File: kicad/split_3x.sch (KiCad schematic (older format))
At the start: 64 parts, among them SW1 SW_Push, SW2 SW_Push, SW3 Rotary_Encoder_Switch, SW4 Rotary_Encoder_Switch, U1 ProMicro, U2 TRRS

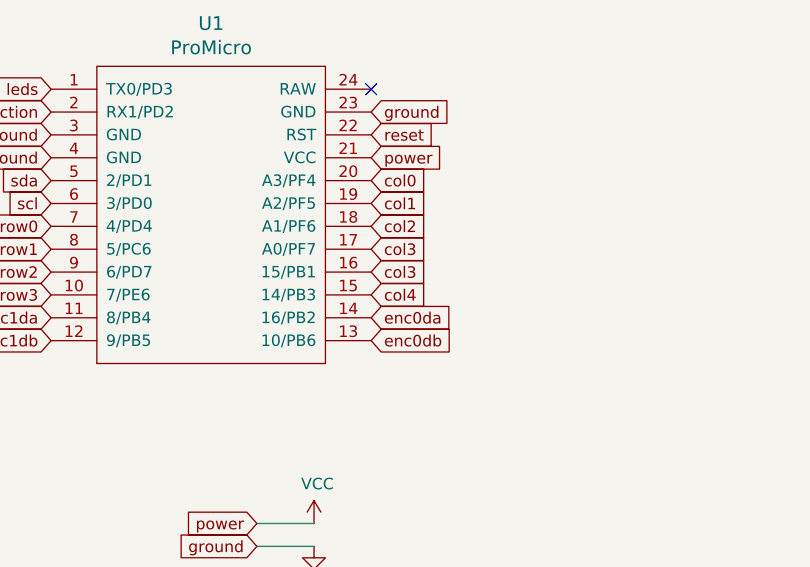
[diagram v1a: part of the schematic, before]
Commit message: added some routing
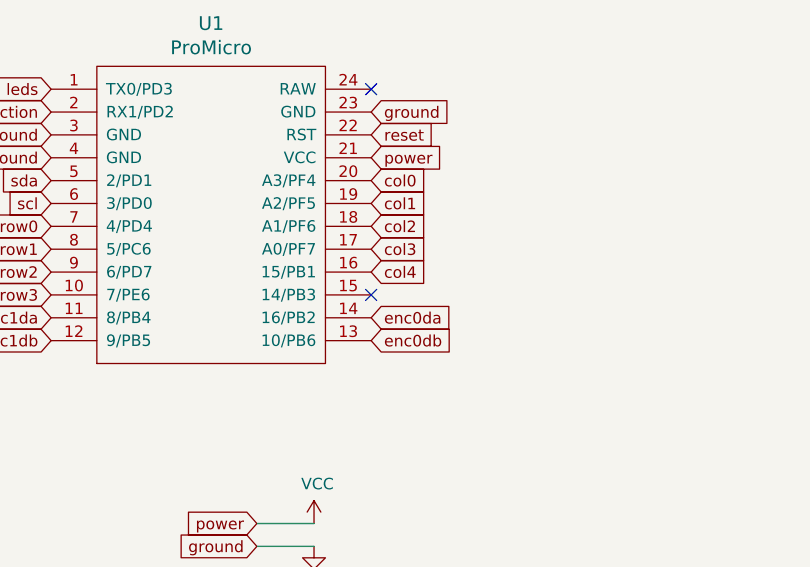
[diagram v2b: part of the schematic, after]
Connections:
- net col3: no longer U1.16 (15/PB1)
- net col4: now also U1.16 (15/PB1); no longer U1.15 (14/PB3)
- no-connect marks 3 -> 4
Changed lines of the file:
@@
 col3
 Text GLabel 2750 2250 2    50   Input ~ 0
-col3
-Text GLabel 2750 2350 2    50   Input ~ 0
 col4
 Text GLabel 1350 2050 0    50   Input ~ 0
@@
 Text GLabel 9750 2250 0    50   Input ~ 0
 power
+NoConn ~ 2750 2350
 $EndSCHEMATC

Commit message: finished routing
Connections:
- net leds: now also D29.4 (DIN); no longer D20.4 (DIN)
- net at D28.2 (DOUT): no longer D29.4 (DIN)
- net at D29.2 (DOUT): now also D20.4 (DIN)
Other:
- moved on the sheet: D29
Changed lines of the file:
@@
 L LED:WS2812B D29
 U 1 1 5FD20037
-P 9650 5550
-F 0 "D29" H 9994 5596 50  0000 L CNN
-F 1 "WS2812B" H 9994 5505 50  0000 L CNN
-F 2 "Keebio-Parts:WS2812B" H 9700 5250 50  0001 L TNN
-F 3 "https://cdn-shop.adafruit.com/datasheets/WS2812B.pdf" H 9750 5175 50  0001 L TNN
-	1    9650 5550
+P 3650 5550
+F 0 "D29" H 3994 5596 50  0000 L CNN
+F 1 "WS2812B" H 3994 5505 50  0000 L CNN
+F 2 "Keebio-Parts:WS2812B" H 3700 5250 50  0001 L TNN
+F 3 "https://cdn-shop.adafruit.com/datasheets/WS2812B.pdf" H 3750 5175 50  0001 L TNN
+	1    3650 5550
 	1    0    0    -1
 $EndComp
@@
 L power:GND #PWR024
 U 1 1 5FD489BC
-P 9650 5850
-F 0 "#PWR024" H 9650 5600 50  0001 C CNN
-F 1 "GND" H 9655 5677 50  0000 C CNN
-F 2 "" H 9650 5850 50  0001 C CNN
-F 3 "" H 9650 5850 50  0001 C CNN
-	1    9650 5850
+P 3650 5850
+F 0 "#PWR024" H 3650 5600 50  0001 C CNN
+F 1 "GND" H 3655 5677 50  0000 C CNN
+F 2 "" H 3650 5850 50  0001 C CNN
+F 3 "" H 3650 5850 50  0001 C CNN
+	1    3650 5850
 	1    0    0    -1
 $EndComp
@@
 L power:VCC #PWR023
 U 1 1 5FD53615
-P 9650 5250
-F 0 "#PWR023" H 9650 5100 50  0001 C CNN
-F 1 "VCC" H 9665 5423 50  0000 C CNN
-F 2 "" H 9650 5250 50  0001 C CNN
-F 3 "" H 9650 5250 50  0001 C CNN
-	1    9650 5250
+P 3650 5250
+F 0 "#PWR023" H 3650 5100 50  0001 C CNN
+F 1 "VCC" H 3665 5423 50  0000 C CNN
+F 2 "" H 3650 5250 50  0001 C CNN
+F 3 "" H 3650 5250 50  0001 C CNN
+	1    3650 5250
 	1    0    0    -1
 $EndComp
 NoConn ~ 9950 5550
-Text GLabel 3950 5550 0    50   Input ~ 0
+Text GLabel 3350 5550 0    50   Input ~ 0
 leds
 $Comp

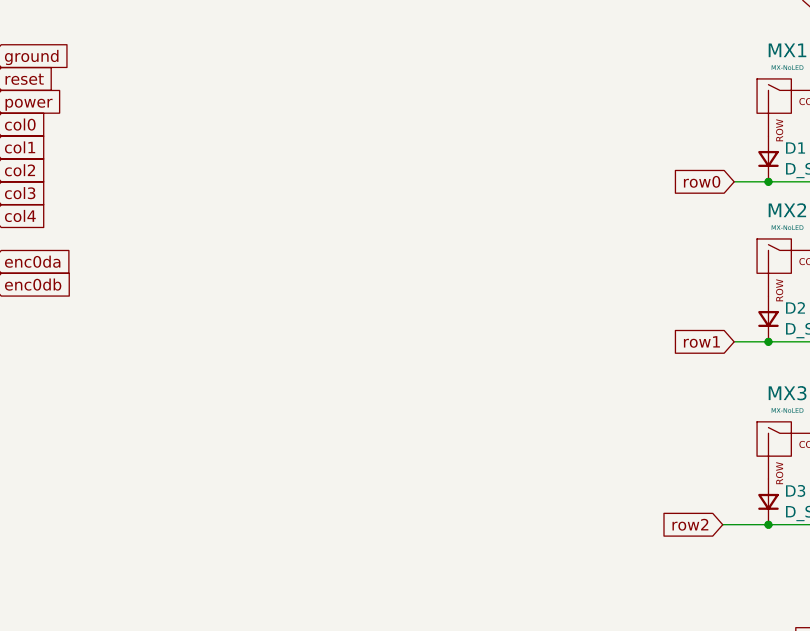
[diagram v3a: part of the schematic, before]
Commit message: added support for the pimoroni trackball breakout, changed a bunch of things, rewired the pcb, changed the bottom plate to be prettier, added some silkscreen, changed the position of one of the mounting holes, changed the angle of the trrs jacks to be properly aligned, changed the top plate to look better
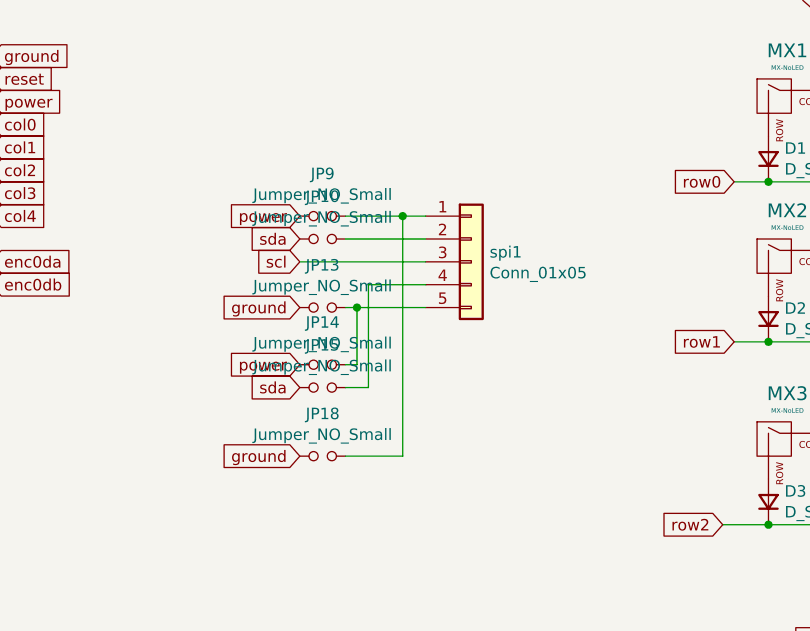
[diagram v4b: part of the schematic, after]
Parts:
- added JP10, JP13, JP14, JP15, JP18, JP9: Jumper_NO_Small, Jumper:SolderJumper-2_P1.3mm_Open_RoundedPad1.0x1.5mm, symbol Device:Jumper_NO_Small
- added spi1: Conn_01x05, other_parts:pimoroni_left_side_mount, symbol Connector_Generic:Conn_01x05
- D1, D10, D11, D12, D13, D14, D15, D16, D17, D18, D19, D2, D3, D4, D5, D6, D7, D8, D9: footprint Keebio-Parts:D_SOD-323 -> Keebio-Parts:D_SOD123F
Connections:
- net GND: now also JP13.1, JP18.1
- net VCC: now also JP14.1, JP9.1
- net scl: now also spi1.3 (Pin_3)
- net sda: now also JP10.1, JP15.1
- new net: JP18.2, JP9.2, spi1.1 (Pin_1)
- new net: JP10.2, spi1.2 (Pin_2)
- new net: JP15.2, spi1.4 (Pin_4)
- new net: JP13.2, JP14.2, spi1.5 (Pin_5)
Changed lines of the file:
@@
 F 0 "D16" V 7846 1930 50  0000 R CNN
 F 1 "D_Small" V 7755 1930 50  0000 R CNN
-F 2 "Keebio-Parts:D_SOD-323" V 7800 2000 50  0001 C CNN
+F 2 "Keebio-Parts:D_SOD123F" V 7800 2000 50  0001 C CNN
 F 3 "~" V 7800 2000 50  0001 C CNN
 	1    7800 2000
@@
 F 0 "D12" V 7446 1930 50  0000 R CNN
 F 1 "D_Small" V 7355 1930 50  0000 R CNN
-F 2 "Keebio-Parts:D_SOD-323" V 7400 2000 50  0001 C CNN
+F 2 "Keebio-Parts:D_SOD123F" V 7400 2000 50  0001 C CNN
 F 3 "~" V 7400 2000 50  0001 C CNN
 	1    7400 2000
@@
 F 0 "D8" V 7046 1930 50  0000 R CNN
 F 1 "D_Small" V 6955 1930 50  0000 R CNN
-F 2 "Keebio-Parts:D_SOD-323" V 7000 2000 50  0001 C CNN
+F 2 "Keebio-Parts:D_SOD123F" V 7000 2000 50  0001 C CNN
 F 3 "~" V 7000 2000 50  0001 C CNN
 	1    7000 2000
@@
 F 0 "D4" V 6646 1930 50  0000 R CNN
 F 1 "D_Small" V 6555 1930 50  0000 R CNN
-F 2 "Keebio-Parts:D_SOD-323" V 6600 2000 50  0001 C CNN
+F 2 "Keebio-Parts:D_SOD123F" V 6600 2000 50  0001 C CNN
 F 3 "~" V 6600 2000 50  0001 C CNN
 	1    6600 2000
@@
 F 0 "D1" V 6196 1930 50  0000 R CNN
 F 1 "D_Small" V 6105 1930 50  0000 R CNN
-F 2 "Keebio-Parts:D_SOD-323" V 6150 2000 50  0001 C CNN
+F 2 "Keebio-Parts:D_SOD123F" V 6150 2000 50  0001 C CNN
 F 3 "~" V 6150 2000 50  0001 C CNN
 	1    6150 2000
@@
 F 0 "D17" V 7846 2630 50  0000 R CNN
 F 1 "D_Small" V 7755 2630 50  0000 R CNN
-F 2 "Keebio-Parts:D_SOD-323" V 7800 2700 50  0001 C CNN
+F 2 "Keebio-Parts:D_SOD123F" V 7800 2700 50  0001 C CNN
 F 3 "~" V 7800 2700 50  0001 C CNN
 	1    7800 2700
@@
 F 0 "D13" V 7446 2630 50  0000 R CNN
 F 1 "D_Small" V 7355 2630 50  0000 R CNN
-F 2 "Keebio-Parts:D_SOD-323" V 7400 2700 50  0001 C CNN
+F 2 "Keebio-Parts:D_SOD123F" V 7400 2700 50  0001 C CNN
 F 3 "~" V 7400 2700 50  0001 C CNN
 	1    7400 2700
@@
 F 0 "D9" V 7046 2630 50  0000 R CNN
 F 1 "D_Small" V 6955 2630 50  0000 R CNN
-F 2 "Keebio-Parts:D_SOD-323" V 7000 2700 50  0001 C CNN
+F 2 "Keebio-Parts:D_SOD123F" V 7000 2700 50  0001 C CNN
 F 3 "~" V 7000 2700 50  0001 C CNN
 	1    7000 2700
@@
 F 0 "D5" V 6646 2630 50  0000 R CNN
 F 1 "D_Small" V 6555 2630 50  0000 R CNN
-F 2 "Keebio-Parts:D_SOD-323" V 6600 2700 50  0001 C CNN
+F 2 "Keebio-Parts:D_SOD123F" V 6600 2700 50  0001 C CNN
 F 3 "~" V 6600 2700 50  0001 C CNN
 	1    6600 2700
@@
 F 0 "D2" V 6196 2630 50  0000 R CNN
 F 1 "D_Small" V 6105 2630 50  0000 R CNN
-F 2 "Keebio-Parts:D_SOD-323" V 6150 2700 50  0001 C CNN
+F 2 "Keebio-Parts:D_SOD123F" V 6150 2700 50  0001 C CNN
 F 3 "~" V 6150 2700 50  0001 C CNN
 	1    6150 2700
@@
 F 0 "D18" V 7846 3430 50  0000 R CNN
 F 1 "D_Small" V 7755 3430 50  0000 R CNN
-F 2 "Keebio-Parts:D_SOD-323" V 7800 3500 50  0001 C CNN
+F 2 "Keebio-Parts:D_SOD123F" V 7800 3500 50  0001 C CNN
 F 3 "~" V 7800 3500 50  0001 C CNN
 	1    7800 3500
@@
 F 0 "D14" V 7446 3430 50  0000 R CNN
 F 1 "D_Small" V 7355 3430 50  0000 R CNN
-F 2 "Keebio-Parts:D_SOD-323" V 7400 3500 50  0001 C CNN
+F 2 "Keebio-Parts:D_SOD123F" V 7400 3500 50  0001 C CNN
 F 3 "~" V 7400 3500 50  0001 C CNN
 	1    7400 3500
@@
 F 0 "D10" V 7046 3430 50  0000 R CNN
 F 1 "D_Small" V 6955 3430 50  0000 R CNN
-F 2 "Keebio-Parts:D_SOD-323" V 7000 3500 50  0001 C CNN
+F 2 "Keebio-Parts:D_SOD123F" V 7000 3500 50  0001 C CNN
 F 3 "~" V 7000 3500 50  0001 C CNN
 	1    7000 3500
@@
 F 0 "D6" V 6646 3430 50  0000 R CNN
 F 1 "D_Small" V 6555 3430 50  0000 R CNN
-F 2 "Keebio-Parts:D_SOD-323" V 6600 3500 50  0001 C CNN
+F 2 "Keebio-Parts:D_SOD123F" V 6600 3500 50  0001 C CNN
 F 3 "~" V 6600 3500 50  0001 C CNN
 	1    6600 3500
@@
 F 0 "D3" V 6196 3430 50  0000 R CNN
 F 1 "D_Small" V 6105 3430 50  0000 R CNN
-F 2 "Keebio-Parts:D_SOD-323" V 6150 3500 50  0001 C CNN
+F 2 "Keebio-Parts:D_SOD123F" V 6150 3500 50  0001 C CNN
 F 3 "~" V 6150 3500 50  0001 C CNN
 	1    6150 3500
@@
 F 0 "D19" V 7846 4130 50  0000 R CNN
 F 1 "D_Small" V 7755 4130 50  0000 R CNN
-F 2 "Keebio-Parts:D_SOD-323" V 7800 4200 50  0001 C CNN
+F 2 "Keebio-Parts:D_SOD123F" V 7800 4200 50  0001 C CNN
 F 3 "~" V 7800 4200 50  0001 C CNN
 	1    7800 4200
@@
 F 0 "D15" V 7446 4130 50  0000 R CNN
 F 1 "D_Small" V 7355 4130 50  0000 R CNN
-F 2 "Keebio-Parts:D_SOD-323" V 7400 4200 50  0001 C CNN
+F 2 "Keebio-Parts:D_SOD123F" V 7400 4200 50  0001 C CNN
 F 3 "~" V 7400 4200 50  0001 C CNN
 	1    7400 4200
@@
 F 0 "D11" V 7046 4130 50  0000 R CNN
 F 1 "D_Small" V 6955 4130 50  0000 R CNN
-F 2 "Keebio-Parts:D_SOD-323" V 7000 4200 50  0001 C CNN
+F 2 "Keebio-Parts:D_SOD123F" V 7000 4200 50  0001 C CNN
 F 3 "~" V 7000 4200 50  0001 C CNN
 	1    7000 4200
@@
 F 0 "D7" V 6696 4130 50  0000 R CNN
 F 1 "D_Small" V 6605 4130 50  0000 R CNN
-F 2 "Keebio-Parts:D_SOD-323" V 6650 4200 50  0001 C CNN
+F 2 "Keebio-Parts:D_SOD123F" V 6650 4200 50  0001 C CNN
 F 3 "~" V 6650 4200 50  0001 C CNN
 	1    6650 4200
@@
 power
 NoConn ~ 2750 2350
+$Comp
+L Connector_Generic:Conn_01x05 spi1
+U 1 1 5FF77D67
+P 4850 2450
+F 0 "spi1" H 4930 2492 50  0000 L CNN
+F 1 "Conn_01x05" H 4930 2401 50  0000 L CNN
+F 2 "other_parts:pimoroni_left_side_mount" H 4850 2450 50  0001 C CNN
+F 3 "~" H 4850 2450 50  0001 C CNN
+	1    4850 2450
+	1    0    0    -1
+$EndComp
+Text GLabel 4100 2650 0    50   Input ~ 0
+ground
+Text GLabel 4100 2250 0    50   Input ~ 0
+power
+$Comp
+L Device:Jumper_NO_Small JP9
+U 1 1 5FF9B084
+P 4200 2250
+F 0 "JP9" H 4200 2435 50  0000 C CNN
+F 1 "Jumper_NO_Small" H 4200 2344 50  0000 C CNN
+F 2 "Jumper:SolderJumper-2_P1.3mm_Open_RoundedPad1.0x1.5mm" H 4200 2250 50  0001 C CNN
+F 3 "~" H 4200 2250 50  0001 C CNN
+	1    4200 2250
+	1    0    0    -1
+$EndComp
+$Comp
+L Device:Jumper_NO_Small JP10
+U 1 1 5FFA2198
+P 4200 2350
+F 0 "JP10" H 4200 2535 50  0000 C CNN
+F 1 "Jumper_NO_Small" H 4200 2444 50  0000 C CNN
+F 2 "Jumper:SolderJumper-2_P1.3mm_Open_RoundedPad1.0x1.5mm" H 4200 2350 50  0001 C CNN
+F 3 "~" H 4200 2350 50  0001 C CNN
+	1    4200 2350
+	1    0    0    -1
+$EndComp
+$Comp
+L Device:Jumper_NO_Small JP13
+U 1 1 5FFA309F
+P 4200 2650
+F 0 "JP13" H 4200 2835 50  0000 C CNN
+F 1 "Jumper_NO_Small" H 4200 2744 50  0000 C CNN
+F 2 "Jumper:SolderJumper-2_P1.3mm_Open_RoundedPad1.0x1.5mm" H 4200 2650 50  0001 C CNN
+F 3 "~" H 4200 2650 50  0001 C CNN
+	1    4200 2650
+	1    0    0    -1
+$EndComp
+$Comp
+L Device:Jumper_NO_Small JP14
+U 1 1 5FFC7519
+P 4200 2900
+F 0 "JP14" H 4200 3085 50  0000 C CNN
+F 1 "Jumper_NO_Small" H 4200 2994 50  0000 C CNN
+F 2 "Jumper:SolderJumper-2_P1.3mm_Open_RoundedPad1.0x1.5mm" H 4200 2900 50  0001 C CNN
+F 3 "~" H 4200 2900 50  0001 C CNN
+	1    4200 2900
+	1    0    0    -1
+$EndComp
+$Comp
+L Device:Jumper_NO_Small JP15
+U 1 1 5FFC751F
+P 4200 3000
+F 0 "JP15" H 4200 3185 50  0000 C CNN
+F 1 "Jumper_NO_Small" H 4200 3094 50  0000 C CNN
+F 2 "Jumper:SolderJumper-2_P1.3mm_Open_RoundedPad1.0x1.5mm" H 4200 3000 50  0001 C CNN
+F 3 "~" H 4200 3000 50  0001 C CNN
+	1    4200 3000
+	1    0    0    -1
+$EndComp
+$Comp
+L Device:Jumper_NO_Small JP18
+U 1 1 5FFC7531
+P 4200 3300
+F 0 "JP18" H 4200 3485 50  0000 C CNN
+F 1 "Jumper_NO_Small" H 4200 3394 50  0000 C CNN
+F 2 "Jumper:SolderJumper-2_P1.3mm_Open_RoundedPad1.0x1.5mm" H 4200 3300 50  0001 C CNN
+F 3 "~" H 4200 3300 50  0001 C CNN
+	1    4200 3300
+	1    0    0    -1
+$EndComp
+Text GLabel 4100 2350 0    50   Input ~ 0
+sda
+Text GLabel 4100 2450 0    50   Input ~ 0
+scl
+Wire Wire Line
+	4300 2650 4350 2650
+Wire Wire Line
+	4300 2900 4350 2900
+Wire Wire Line
+	4350 2900 4350 2650
+Connection ~ 4350 2650
+Wire Wire Line
+	4350 2650 4650 2650
+Wire Wire Line
+	4300 3000 4400 3000
+Wire Wire Line
+	4400 2550 4650 2550
+Wire Wire Line
+	4300 2250 4550 2250
+Wire Wire Line
+	4300 3300 4550 3300
+Wire Wire Line
+	4550 3300 4550 2250
+Connection ~ 4550 2250
+Wire Wire Line
+	4550 2250 4650 2250
+Text GLabel 4100 3300 0    50   Input ~ 0
+ground
+Text GLabel 4100 2900 0    50   Input ~ 0
+power
+Text GLabel 4100 3000 0    50   Input ~ 0
+sda
+Wire Wire Line
+	4100 2450 4650 2450
+Wire Wire Line
+	4300 2350 4650 2350
+Wire Wire Line
+	4400 2550 4400 3000
 $EndSCHEMATC

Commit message: adde a footprint to solder a battery and smd switches to toggle it
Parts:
- added BT1: Bat_loc1, Connector_JST:JST_PH_S2B-PH-K_1x02_P2.00mm_Horizontal, symbol Device:Battery_Cell
- added SW5, SW6: SW_DIP_x01, other_parts:switch_MSK-12C02_smd, symbol Switch:SW_DIP_x01
- Brd1: symbol SSD1306-128x64_OLED:SSD1306 -> split_3x-rescue:SSD1306-SSD1306-128x64_OLED
- MX1, MX10, MX11, MX12, MX13, MX14, MX15, MX16, MX17, MX18, MX2, MX3, MX4, MX5, MX6, MX7, MX8, MX9: symbol MX_Alps_Hybrid:MX-NoLED -> split_3x-rescue:MX-NoLED-MX_Alps_Hybrid
- U1: symbol keebio:ProMicro -> split_3x-rescue:ProMicro-keebio
- U2: symbol keebio:TRRS -> split_3x-rescue:TRRS-keebio
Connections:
- net GND: now also BT1.2 (-)
- net raw: now reaches U1.24 (RAW)
- net raw: now also SW5.2, SW6.2
- new net: BT1.1 (+), SW5.1, SW6.1
- no-connect marks 4 -> 3
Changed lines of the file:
@@
 $EndDescr
 $Comp
-L keebio:ProMicro U1
+L split_3x-rescue:ProMicro-keebio U1
 U 1 1 5FB16BB9
 P 2050 2000
@@
 $EndComp
 $Comp
-L MX_Alps_Hybrid:MX-NoLED MX1
+L split_3x-rescue:MX-NoLED-MX_Alps_Hybrid MX1
 U 1 1 5FB323B1
 P 6200 1750
@@
 $EndComp
 $Comp
-L MX_Alps_Hybrid:MX-NoLED MX4
+L split_3x-rescue:MX-NoLED-MX_Alps_Hybrid MX4
 U 1 1 5FB3417F
 P 6650 1750
@@
 $EndComp
 $Comp
-L MX_Alps_Hybrid:MX-NoLED MX7
+L split_3x-rescue:MX-NoLED-MX_Alps_Hybrid MX7
 U 1 1 5FB34604
 P 7050 1750
@@
 $EndComp
 $Comp
-L MX_Alps_Hybrid:MX-NoLED MX11
+L split_3x-rescue:MX-NoLED-MX_Alps_Hybrid MX11
 U 1 1 5FB34B53
 P 7450 1750
@@
 $EndComp
 $Comp
-L MX_Alps_Hybrid:MX-NoLED MX15
+L split_3x-rescue:MX-NoLED-MX_Alps_Hybrid MX15
 U 1 1 5FB35275
 P 7850 1750
@@
 $EndComp
 $Comp
-L MX_Alps_Hybrid:MX-NoLED MX2
+L split_3x-rescue:MX-NoLED-MX_Alps_Hybrid MX2
 U 1 1 5FB37E94
 P 6200 2450
@@
 $EndComp
 $Comp
-L MX_Alps_Hybrid:MX-NoLED MX5
+L split_3x-rescue:MX-NoLED-MX_Alps_Hybrid MX5
 U 1 1 5FB37E9A
 P 6650 2450
@@
 $EndComp
 $Comp
-L MX_Alps_Hybrid:MX-NoLED MX8
+L split_3x-rescue:MX-NoLED-MX_Alps_Hybrid MX8
 U 1 1 5FB37EA0
 P 7050 2450
@@
 $EndComp
 $Comp
-L MX_Alps_Hybrid:MX-NoLED MX12
+L split_3x-rescue:MX-NoLED-MX_Alps_Hybrid MX12
 U 1 1 5FB37EA6
 P 7450 2450
@@
 $EndComp
 $Comp
-L MX_Alps_Hybrid:MX-NoLED MX16
+L split_3x-rescue:MX-NoLED-MX_Alps_Hybrid MX16
 U 1 1 5FB37EAC
 P 7850 2450
@@
 $EndComp
 $Comp
-L MX_Alps_Hybrid:MX-NoLED MX3
+L split_3x-rescue:MX-NoLED-MX_Alps_Hybrid MX3
 U 1 1 5FB39317
 P 6200 3250
@@
 $EndComp
 $Comp
-L MX_Alps_Hybrid:MX-NoLED MX6
+L split_3x-rescue:MX-NoLED-MX_Alps_Hybrid MX6
 U 1 1 5FB3931D
 P 6650 3250
@@
 $EndComp
 $Comp
-L MX_Alps_Hybrid:MX-NoLED MX9
+L split_3x-rescue:MX-NoLED-MX_Alps_Hybrid MX9
 U 1 1 5FB39323
 P 7050 3250
@@
 $EndComp
 $Comp
-L MX_Alps_Hybrid:MX-NoLED MX13
+L split_3x-rescue:MX-NoLED-MX_Alps_Hybrid MX13
 U 1 1 5FB39329
 P 7450 3250
@@
 $EndComp
 $Comp
-L MX_Alps_Hybrid:MX-NoLED MX17
+L split_3x-rescue:MX-NoLED-MX_Alps_Hybrid MX17
 U 1 1 5FB3932F
 P 7850 3250
@@
 $EndComp
 $Comp
-L MX_Alps_Hybrid:MX-NoLED MX10
+L split_3x-rescue:MX-NoLED-MX_Alps_Hybrid MX10
 U 1 1 5FB426A8
 P 7050 3950
@@
 $EndComp
 $Comp
-L MX_Alps_Hybrid:MX-NoLED MX14
+L split_3x-rescue:MX-NoLED-MX_Alps_Hybrid MX14
 U 1 1 5FB426AE
 P 7450 3950
@@
 $EndComp
 $Comp
-L MX_Alps_Hybrid:MX-NoLED MX18
+L split_3x-rescue:MX-NoLED-MX_Alps_Hybrid MX18
 U 1 1 5FB426B4
 P 7850 3950
@@
 Text GLabel 2750 1650 2    50   Input ~ 0
 reset
-NoConn ~ 2750 1450
 Text GLabel 1350 1450 0    50   Input ~ 0
 leds
@@
 $EndComp
 $Comp
-L SSD1306-128x64_OLED:SSD1306 Brd1
+L split_3x-rescue:SSD1306-SSD1306-128x64_OLED Brd1
 U 1 1 5FCA781D
 P 3200 6500
@@
 leds
 $Comp
-L keebio:TRRS U2
+L split_3x-rescue:TRRS-keebio U2
 U 1 1 5FD948D1
 P 10100 2650
@@
 Wire Wire Line
 	4400 2550 4400 3000
+$Comp
+L Device:Battery_Cell BT1
+U 1 1 6114E51A
+P 3850 1450
+F 0 "BT1" H 3968 1546 50  0000 L CNN
+F 1 "Bat_loc1" H 3968 1455 50  0000 L CNN
+F 2 "Connector_JST:JST_PH_S2B-PH-K_1x02_P2.00mm_Horizontal" V 3850 1510 50  0001 C CNN
+F 3 "~" V 3850 1510 50  0001 C CNN
+	1    3850 1450
+	1    0    0    -1
+$EndComp
+$Comp
+L Switch:SW_DIP_x01 SW5
+U 1 1 6116D831
+P 5150 1250
+F 0 "SW5" H 5150 1517 50  0000 C CNN
+F 1 "SW_DIP_x01" H 5150 1426 50  0000 C CNN
+F 2 "other_parts:switch_MSK-12C02_smd" H 5150 1250 50  0001 C CNN
+F 3 "~" H 5150 1250 50  0001 C CNN
+	1    5150 1250
+	1    0    0    -1
+$EndComp
+Text GLabel 3700 1550 0    50   Input ~ 0
+ground
+Wire Wire Line
+	3700 1550 3850 1550
+Text GLabel 2750 1450 2    50   Input ~ 0
+raw
+Text GLabel 5450 1250 2    50   Input ~ 0
+raw
+$Comp
+L Switch:SW_DIP_x01 SW6
+U 1 1 610FB382
+P 5150 1650
+F 0 "SW6" H 5150 1917 50  0000 C CNN
+F 1 "SW_DIP_x01" H 5150 1826 50  0000 C CNN
+F 2 "other_parts:switch_MSK-12C02_smd" H 5150 1650 50  0001 C CNN
+F 3 "~" H 5150 1650 50  0001 C CNN
+	1    5150 1650
+	1    0    0    -1
+$EndComp
+Wire Wire Line
+	4850 1250 4850 1650
+Connection ~ 4850 1250
+Wire Wire Line
+	5450 1650 5450 1250
+Wire Wire Line
+	3850 1250 4850 1250
 $EndSCHEMATC

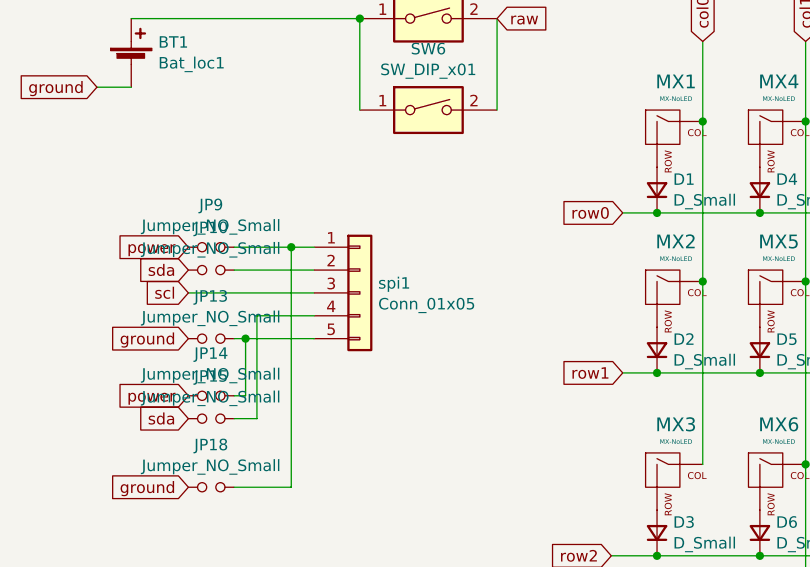
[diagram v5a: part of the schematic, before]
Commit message: modified the silkscreen to work better with the battery
:
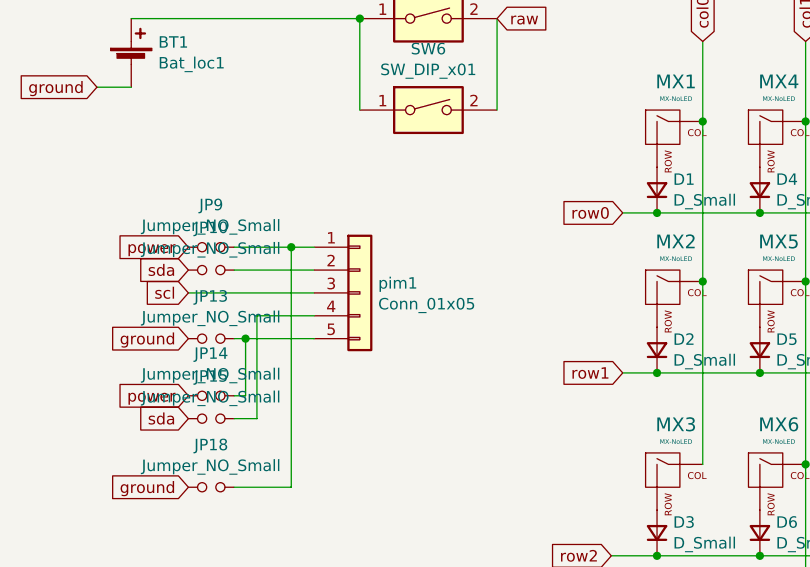
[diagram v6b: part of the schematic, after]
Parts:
- BT1: footprint Connector_JST:JST_PH_S2B-PH-K_1x02_P2.00mm_Horizontal -> Connector_PinHeader_2.00mm:PinHeader_1x02_P2.00mm_Vertical
- renumbered spi1 to pim1
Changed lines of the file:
@@
 NoConn ~ 2750 2350
 $Comp
-L Connector_Generic:Conn_01x05 spi1
+L Connector_Generic:Conn_01x05 pim1
 U 1 1 5FF77D67
 P 4850 2450
-F 0 "spi1" H 4930 2492 50  0000 L CNN
+F 0 "pim1" H 4930 2492 50  0000 L CNN
 F 1 "Conn_01x05" H 4930 2401 50  0000 L CNN
 F 2 "other_parts:pimoroni_left_side_mount" H 4850 2450 50  0001 C CNN
@@
 F 0 "BT1" H 3968 1546 50  0000 L CNN
 F 1 "Bat_loc1" H 3968 1455 50  0000 L CNN
-F 2 "Connector_JST:JST_PH_S2B-PH-K_1x02_P2.00mm_Horizontal" V 3850 1510 50  0001 C CNN
+F 2 "Connector_PinHeader_2.00mm:PinHeader_1x02_P2.00mm_Vertical" V 3850 1510 50  0001 C CNN
 F 3 "~" V 3850 1510 50  0001 C CNN
 	1    3850 1450
